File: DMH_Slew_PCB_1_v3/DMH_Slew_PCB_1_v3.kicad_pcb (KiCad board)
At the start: 2 copper layers, 48 x 175 mm, 33 parts, among them J0 Conn_01x01, J1 TS_Jack_6.35mm_Sw, J10 TS_Jack_6.35mm_Sw, J100 IDC_02x08, J14 Conn_02x03_Top_Bottom, J15 Conn_02x06_Top_Bottom, J16 Conn_02x03_Top_Bottom, J17 Conn_01x08, J18 Conn_01x08, J2 TS_Jack_6.35mm_Sw, J200 IDC_02x05, J24 Conn_02x03_Top_Bottom, J25 Conn_02x06_Top_Bottom, J26 Conn_02x03_Top_Bottom, J27 Conn_01x08, J28 Conn_01x08, J3 TS_Jack_6.35mm_Sw, J4 TS_Jack_6.35mm_Sw, J5 TS_Jack_6.35mm_Sw, J6 TS_Jack_6.35mm_Sw, J7 TS_Jack_6.35mm_Sw, J8 TS_Jack_6.35mm_Sw, J9 TS_Jack_6.35mm_Sw, U10 LM4040LP-10, U11 LM4040LP-10

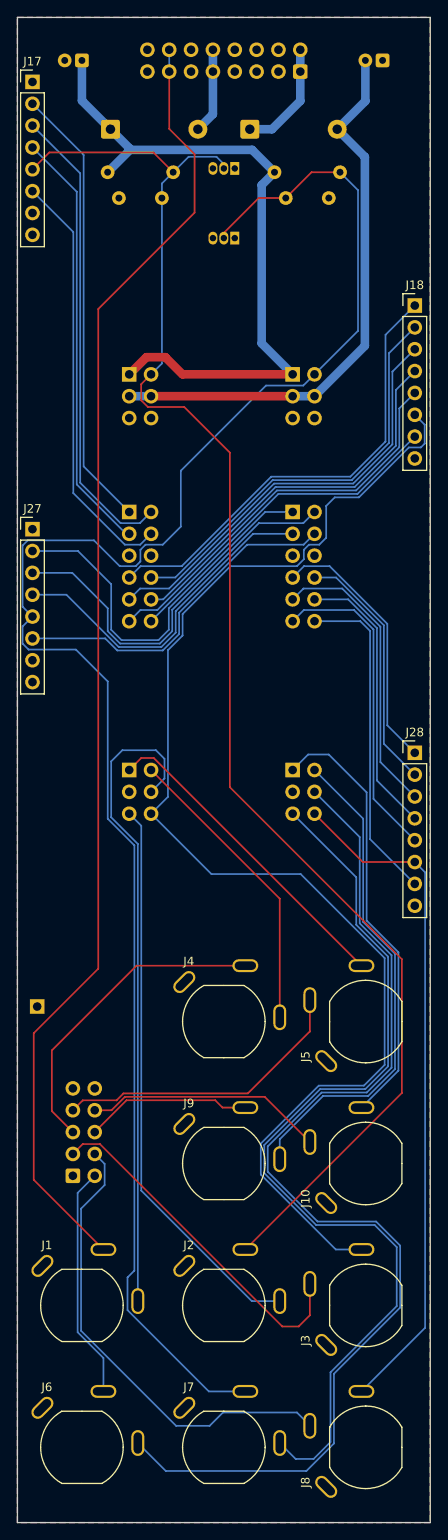
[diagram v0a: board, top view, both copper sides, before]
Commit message: Exposed loopback resistor to submodule connector
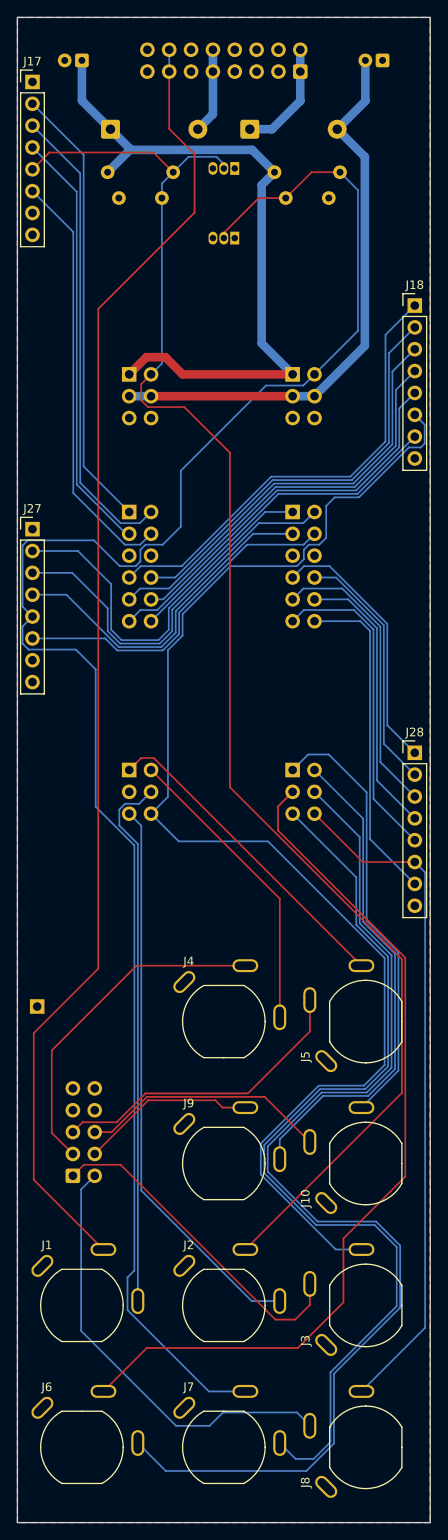
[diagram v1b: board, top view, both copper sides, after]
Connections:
- J200 pad 1: unconnected-(J200-Pin_1-Pad1) -> A_Out_Jack_TN_M
- J200 pad 2: A_Out_Jack_TN_M -> A_R_Gate_Jack_TN_M
- J200 pad 3: A_R_Gate_Jack_TN_M -> A_F_Gate_Jack_TN_M
- J200 pad 4: A_F_Gate_Jack_TN_M -> GND
- J200 pad 6: B_Input_Jack_TN_M -> B_Out_Jack_TN_M
- J200 pad 7: B_Out_Jack_TN_M -> B_R_Gate_Jack_TN_M
- J200 pad 8: B_R_Gate_Jack_TN_M -> B_F_Gate_Jack_TN_M
- J200 pad 9: B_F_Gate_Jack_TN_M -> GND
- J26 pad 3: GND -> B_Loopback_M
- J6 pad TN: B_Input_Jack_TN_M -> B_Loopback_M
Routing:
- net B_Loopback_M: track 0.00 -> 101.4 mm
- net B_Input_Jack_TN_M: track 27.1 -> 0.00 mm
- net A_Input_Jack_M: track 75.7 -> 62.6 mm
- net B_Out_Jack_TN_M: track 54.7 -> 51.2 mm
- net A_R_Gate_Jack_TN_M: track 37.1 -> 39.6 mm
- net A_Out_Jack_TN_M: track 41.0 -> 38.7 mm
- net B_R_Gate_Jack_TN_M: track 19.4 -> 20.4 mm
- net B_F_Gate_Jack_TN_M: track 27.8 -> 28.9 mm
- net A_F_Gate_Jack_TN_M: track 35.0 -> 36.0 mm

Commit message: Generated Gerbers
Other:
- board text added: "Mk1.0 - March 2026"
- board text removed: "Mk1.0 - Month Year"
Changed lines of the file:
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@@
 			(plot_on_all_layers_selection 0x00000000_00000000_00000000_00000000)
 			(disableapertmacros no)
-			(usegerberextensions no)
+			(usegerberextensions yes)
 			(usegerberattributes yes)
 			(usegerberadvancedattributes yes)
@@
 			(sketchdnponfab yes)
 			(crossoutdnponfab yes)
-			(subtractmaskfromsilk no)
+			(subtractmaskfromsilk yes)
 			(outputformat 1)
 			(mirror no)
-			(drillshape 1)
+			(drillshape 0)
 			(scaleselection 1)
-			(outputdirectory "")
+			(outputdirectory "Gerbers/")
 		)
 	)
@@
 		(layer "User.9")
 	)
-	(gr_text "Mk1.0 - Month Year"
+	(gr_text "Mk1.0 - March 2026"
 		(at 74.75 216.5 0)
 		(layer "B.SilkS")

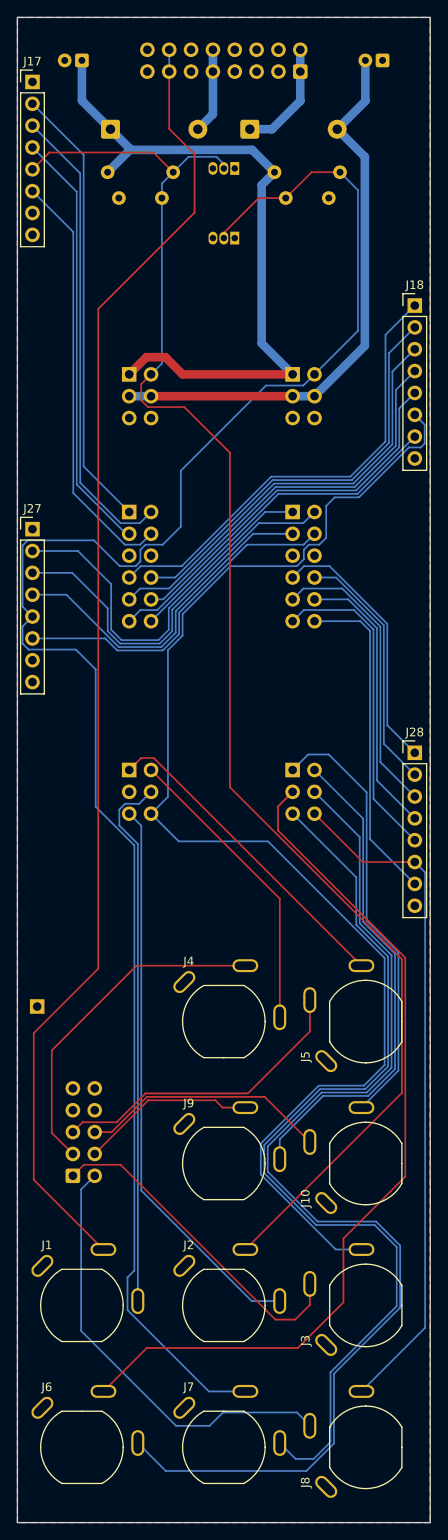
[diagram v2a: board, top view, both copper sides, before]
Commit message: Redesigned Main PCB
and regenerated Gerbers
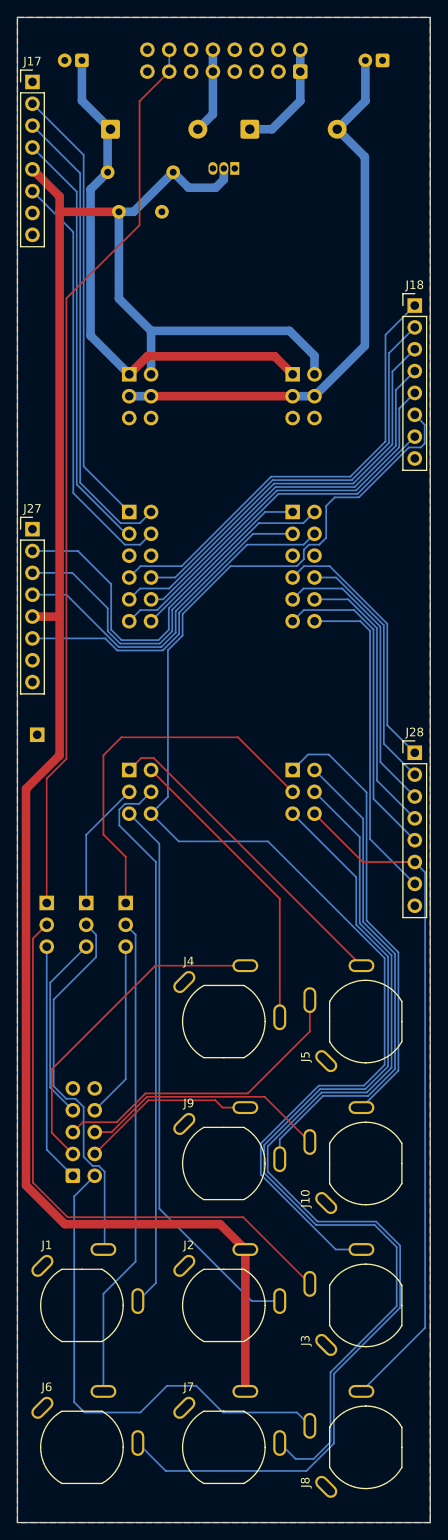
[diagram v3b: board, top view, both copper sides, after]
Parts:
- removed C16: 100nF, Capacitor_THT:C_Disc_D4.3mm_W1.9mm_P5.00mm
- removed R45: 1k, Resistor_THT:R_Axial_DIN0207_L6.3mm_D2.5mm_P7.62mm_Horizontal
- removed U11: LM4040LP-10, Package_TO_SOT_THT:TO-92_Inline
- added JP1: Jumper_3_Bridged12, Connector_PinHeader_2.54mm:PinHeader_1x03_P2.54mm_Vertical, B.Cu at (54.4, 145.5)
- added JP2: Jumper_3_Bridged12, Connector_PinHeader_2.54mm:PinHeader_1x03_P2.54mm_Vertical, B.Cu at (59.0, 145.5)
- added JP3: Jumper_3_Bridged12, Connector_PinHeader_2.54mm:PinHeader_1x03_P2.54mm_Vertical, B.Cu at (63.6, 145.5)
- R49: value 1k -> 470R
- moved J0 31.6 mm to (53.3, 125.9)
- moved C5 5.25 mm to (62.8, 65.1), turned to 0 degrees
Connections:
- C5 pad 1: +10V_A -> +10V
- J1 pad TN: Bus_CV_M -> A_In_Jack_TN_M
- J14 pad 2: +10V_A -> +10V
- J16 pad 3: GND -> A_Loopback_M
- J17 pad 5: +10V_A -> +10V
- J2 pad TN: +10V_A -> +10V
- J200 pad 1: A_Out_Jack_TN_M -> Net-(J200-Pin_1)
- J200 pad 4: GND -> Net-(J200-Pin_4)
- J200 pad 9: GND -> Net-(J200-Pin_9)
- J24 pad 2: +10V_B -> +10V
- J27 pad 5: +10V_B -> +10V
- J6 pad TN: B_Loopback_M -> B_In_Jack_TN_M
- J7 pad TN: +10V_B -> +10V
- R49 pad 1: +10V_A -> +10V
- U10 pad 2: +10V_A -> +10V
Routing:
- net +10V: track 0.00 -> 235.6 mm
- net +10V_B: track 209.2 -> 0.00 mm
- net +10V_A: track 175.0 -> 0.00 mm
- net B_Loopback_M: track 101.4 -> 43.7 mm
- net B_In_Jack_TN_M: track 0.00 -> 56.3 mm
- net Bus_CV_M: track 151.8 -> 105.1 mm
- net A_In_Jack_TN_M: track 0.00 -> 43.8 mm
- net A_Out_Jack_TN_M: track 38.7 -> 67.7 mm
- net Net-(J200-Pin_1): track 0.00 -> 27.9 mm
- net Net-(J200-Pin_4): track 0.00 -> 21.8 mm
- net Net-(J200-Pin_9): track 0.00 -> 20.5 mm
- net +12V: track 80.5 -> 61.4 mm
- net A_Loopback_M: track 0.00 -> 15.0 mm
- net B_Out_Jack_TN_M: track 51.2 -> 58.4 mm
- net A_Input_Jack_M: track 62.6 -> 64.3 mm
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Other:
- board text added: "Bus CV"
- board text added: "Jumpers"
- board text added: "LFO"
- board text added: "Mk1.1 - April 2026"
- board text removed: "Mk1.0 - March 2026"
